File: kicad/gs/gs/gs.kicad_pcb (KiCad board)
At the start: 2 copper layers, 198 x 198 mm, 54 parts, among them J1 Jack_12V, J2 JST_MotorAz, J3 JST_MotorEl, J4 Conn_02x10_Odd_Even, J5 PowerBreakout, J6 JST_ZeroAZ, U1 ESP32-WROOM-32-DEV, U2 MPU-9250-DEV, U3 Ai-Thinker-Ra-02, U4 L7805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

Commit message: Exported GS Rev 4 Gerbers
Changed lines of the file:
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@@
       (outputformat 1)
       (mirror false)
-      (drillshape 1)
+      (drillshape 0)
       (scaleselection 1)
       (outputdirectory "")
@@
     (fp_line (start 9.95 2.8) (end 9.95 -1.7)
       (stroke (width 0.1) (type solid)) (layer "F.Fab"))
-    (pad "1" thru_hole roundrect (at 0 0) (size 1.2 1.75) (drill 0.75) (layers "*.Cu" "*.Mask") (roundrect_rratio 0.208333)
+    (pad "1" thru_hole roundrect (at 0 0) (size 1.2 1.75) (drill 0.75) (layers "*.Cu" "*.Mask") (roundrect_rratio 0.2083333333)
       (net 2 "GND") (pinfunction "Pin_1") (pintype "passive"))
     (pad "2" thru_hole oval (at 2 0) (size 1.2 1.75) (drill 0.75) (layers "*.Cu" "*.Mask")
@@
     (fp_line (start 7.95 2.8) (end 7.95 -1.7)
       (stroke (width 0.1) (type solid)) (layer "F.Fab"))
-    (pad "1" thru_hole roundrect (at 0 0 270) (size 1.2 1.75) (drill 0.75) (layers "*.Cu" "*.Mask") (roundrect_rratio 0.208333)
+    (pad "1" thru_hole roundrect (at 0 0 270) (size 1.2 1.75) (drill 0.75) (layers "*.Cu" "*.Mask") (roundrect_rratio 0.2083333333)
       (net 59 "M1_1B") (pinfunction "Pin_1") (pintype "passive"))
     (pad "2" thru_hole oval (at 2 0 270) (size 1.2 1.75) (drill 0.75) (layers "*.Cu" "*.Mask")
@@
     (fp_line (start 7.95 2.8) (end 7.95 -1.7)
       (stroke (width 0.1) (type solid)) (layer "F.Fab"))
-    (pad "1" thru_hole roundrect (at 0 0 270) (size 1.2 1.75) (drill 0.75) (layers "*.Cu" "*.Mask") (roundrect_rratio 0.208333)
+    (pad "1" thru_hole roundrect (at 0 0 270) (size 1.2 1.75) (drill 0.75) (layers "*.Cu" "*.Mask") (roundrect_rratio 0.2083333333)
       (net 63 "M2_1B") (pinfunction "Pin_1") (pintype "passive"))
     (pad "2" thru_hole oval (at 2 0 270) (size 1.2 1.75) (drill 0.75) (layers "*.Cu" "*.Mask")

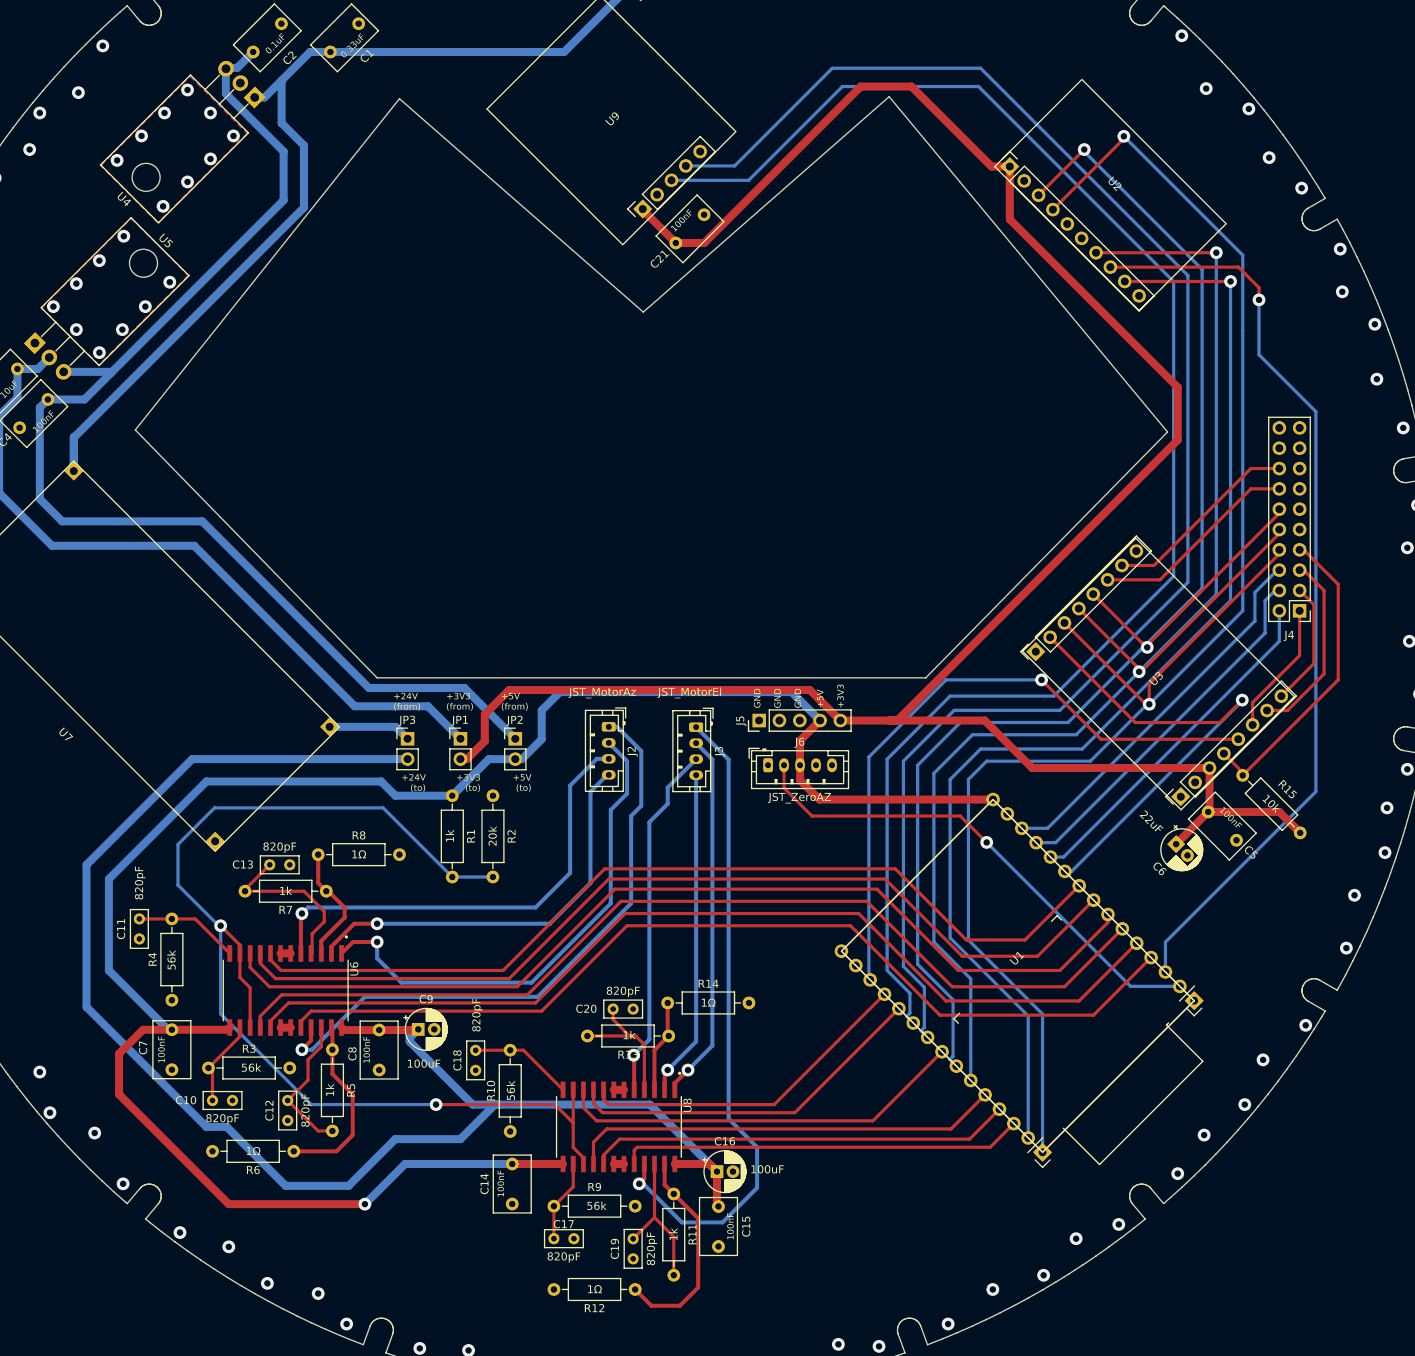
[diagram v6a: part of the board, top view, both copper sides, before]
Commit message: Fixed GS PCB Rev 4 problems to be Rev 4.1
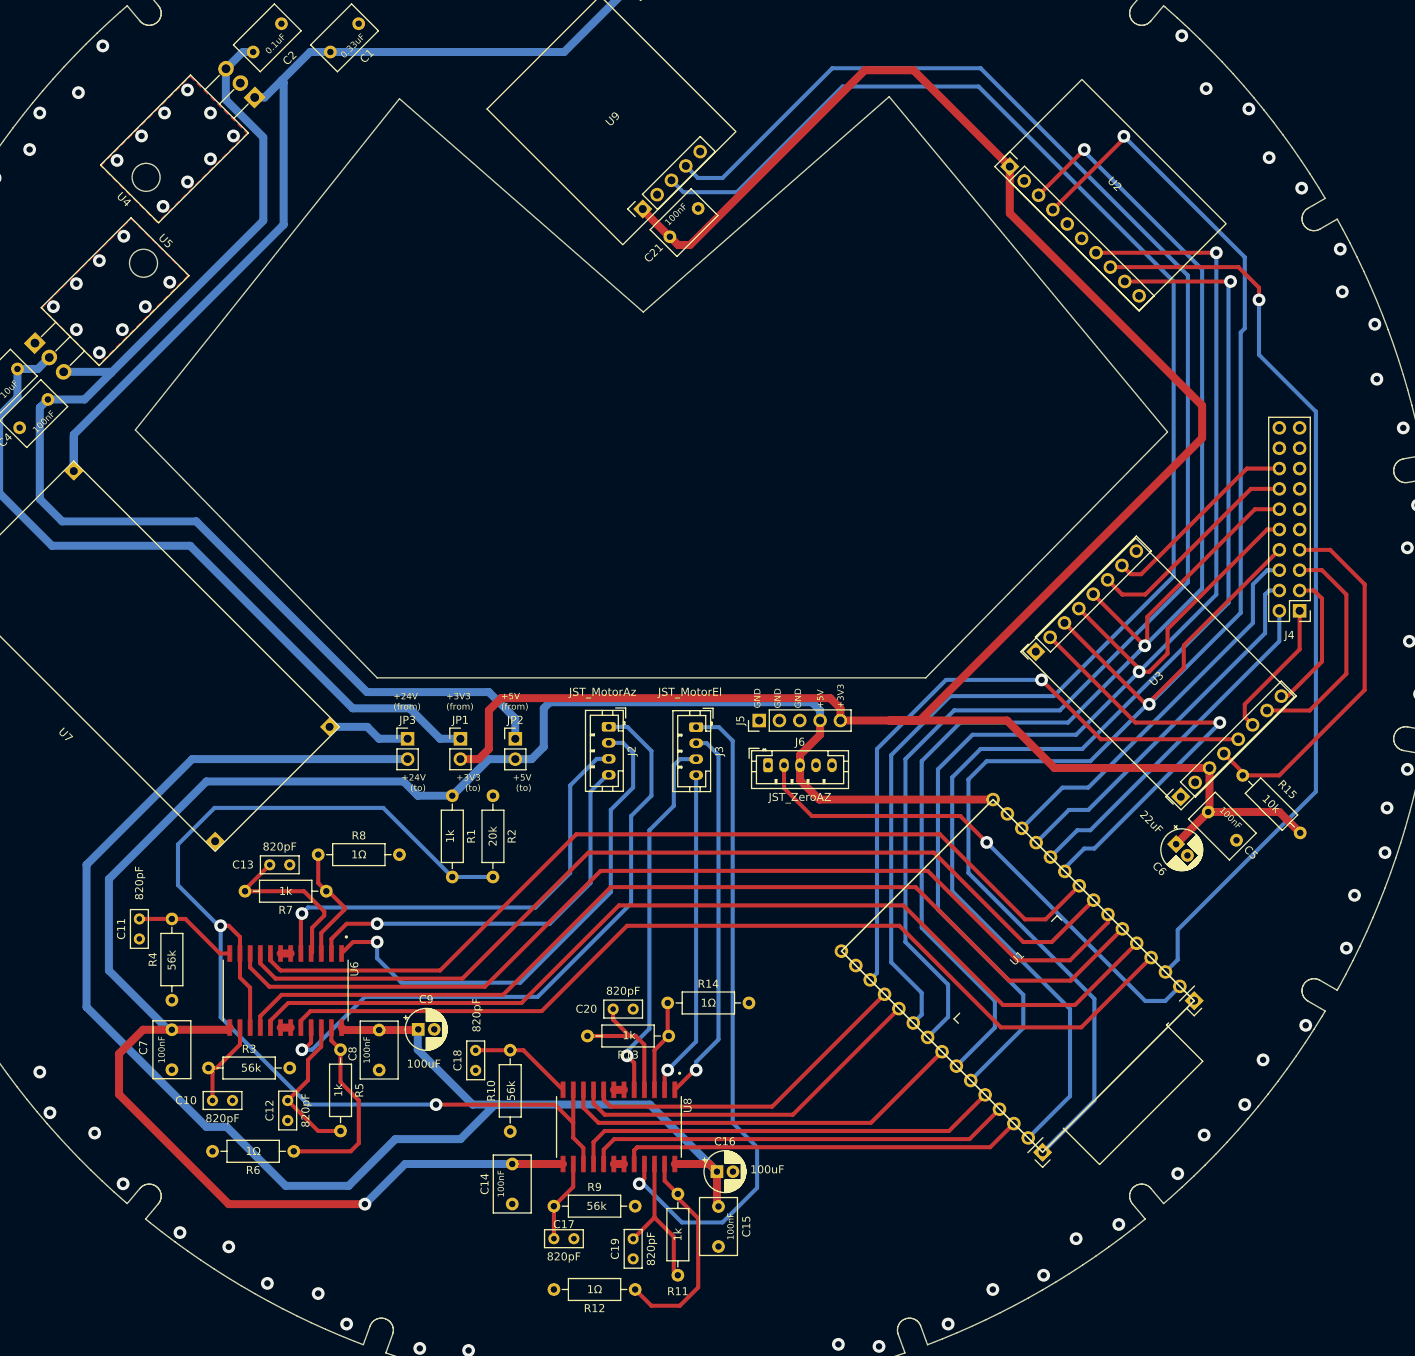
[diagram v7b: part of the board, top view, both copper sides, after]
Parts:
- moved C21 1.08 mm to (216.7, 98.5)
- moved R5 1.02 mm to (175.5, 200.2)
- moved R11 0.51 mm to (217.7, 218.2)
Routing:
- net RF_NSS: track 60.7 -> 53.0 mm
- net RF_NRESET: track 39.1 -> 46.5 mm
- net +3V3: track 280.5 -> 287.4 mm
- net SPI_MISO: track 178.8 -> 185.3 mm
- net SPI_MOSI: track 212.6 -> 218.2 mm
- net RF_DIO2: track 23.6 -> 28.8 mm
- net SPI_SCK: track 188.6 -> 192.9 mm
- net IMU_NSS: track 146.3 -> 150.4 mm
- net GPS_RX: track 197.8 -> 200.7 mm
- net RF_DIO3: track 15.6 -> 18.0 mm
- net +12V: track 121.5 -> 119.4 mm
- net M1_1B: track 76.8 -> 78.8 mm
- net M2_2B: track 44.6 -> 46.5 mm
- net M2_1B: track 82.0 -> 83.7 mm
- net /M1_Sense1_In: track 22.7 -> 24.4 mm
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- added copper zone on F.Cu, net Heatsink3V3
- added copper zone on F.Cu, net Heatsink5V
- removed copper zone on F.Cu, net (none)
